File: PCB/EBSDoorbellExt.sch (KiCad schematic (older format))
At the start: 35 parts

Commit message: Completed the initial layout and Gerbers
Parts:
- removed U?: LM555N, symbol LM555N
- added U2: LM555N, Housings_SOIC:SOIC-8_3.9x4.9mm_Pitch1.27mm, symbol LM555N
- C1: renamed from C?; footprint (none) -> Capacitors_ThroughHole:C_Radial_D10_L13_P5
- C10: renamed from C?; footprint 1206 -> Capacitors_SMD:C_1206_HandSoldering
- C2, C3, C5, C6, C7, C8: renamed from C?; footprint (none) -> Capacitors_SMD:C_0805_HandSoldering
- C4, C9: renamed from C?; footprint (none) -> Capacitors_ThroughHole:C_Radial_D5_L11_P2
- D1, D4, D6: renamed from D?; footprint (none) -> Diodes_SMD:SOD-523
- D2: renamed from D?; footprint (none) -> EBSDoorbellExt-Footprints:B80C1500G
- D3, D5: renamed from D?; footprint (none) -> LEDs:LED_0805
- MOD1: renamed from MOD?; footprint (none) -> EBSDoorbellExt-Footprints:BoardConnector_Horizontal_1x2_P5; symbol FS20S4SUB2/4 -> FS20S4SUB2/4-RESCUE-EBSDoorbellExt
- P1: renamed from P?; value CONN_01X02 -> AC in; footprint (none) -> EBSDoorbellExt-Footprints:BoardConnector_Horizontal_1x2_P5; ConradPN (none) -> Value; DigiKeyPN (none) -> Value; Link (none) -> Value; Voltage (none) -> Value
- P2: renamed from P?; value CONN_01X03 -> Doorbell; footprint (none) -> EBSDoorbellExt-Footprints:BoardConnector_Horizontal_1x3_P5; ConradPN (none) -> Value; DigiKeyPN (none) -> Value; Link (none) -> Value; Voltage (none) -> Value
- Q1: renamed from Q?; footprint (none) -> TO_SOT_Packages_SMD:SOT-23
- R1, R10, R2, R3, R4, R5, R6, R7, R8, R9: renamed from R?; footprint (none) -> Resistors_SMD:R_0805_HandSoldering
- REL1: renamed from REL?; footprint (none) -> EBSDoorbellExt-Footprints:MES1A12
- SW1: renamed from SW?; footprint (none) -> Pin_Headers:Pin_Header_Straight_1x02
- SW2: renamed from SW?; footprint (none) -> EBSDoorbellExt-Footprints:FSM2JSMAA
- U1: renamed from U?; footprint TO-220 -> TO_SOT_Packages_THT:TO-220_Neutral123_Vertical
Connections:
- net labels added: In1
- wire segments 85 -> 87
- no-connect marks 3 -> 0
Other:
- moved on the sheet: R6

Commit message: Updated the layout to include the heatsink
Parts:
- removed P2: Doorbell, EBSDoorbellExt-Footprints:BoardConnector_Horizontal_1x3_P5, symbol CONN_01X03
- added P2: Doorbell, EBSDoorbellExt-Footprints:BoardConnector_Horizontal_1x3_P5, symbol Doorbell
- R6: footprint Resistors_SMD:R_0805_HandSoldering -> Resistors_SMD:R_1812_HandSoldering; DigiKeyPN Value -> MF-MSMF050-2CT-ND
- REL1: ConradPN (none) -> Value; DigiKeyPN (none) -> Value; Link (none) -> Value; Voltage (none) -> Value
- U1: value LM7809ACT -> LM7812CT; DigiKeyPN MC7809CTGOS-ND -> LM7812CTFS-ND
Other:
- note added: "Optional"
- moved on the sheet: C7, C8, C9, D4, D6, Q1, R10, R4, R6, R7, R8, R9

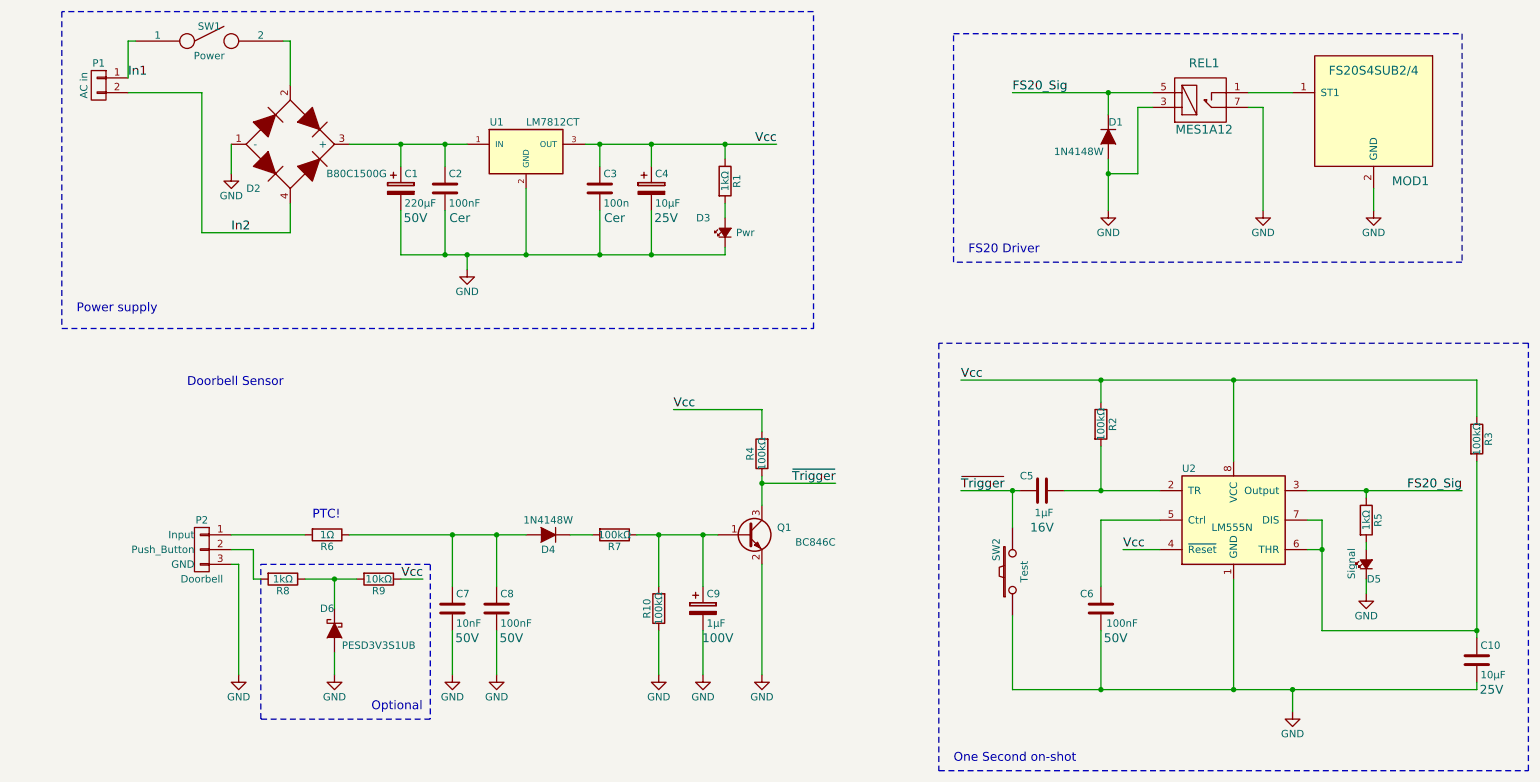
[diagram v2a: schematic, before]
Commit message: Added some test points and moved the LEDs help with the casing
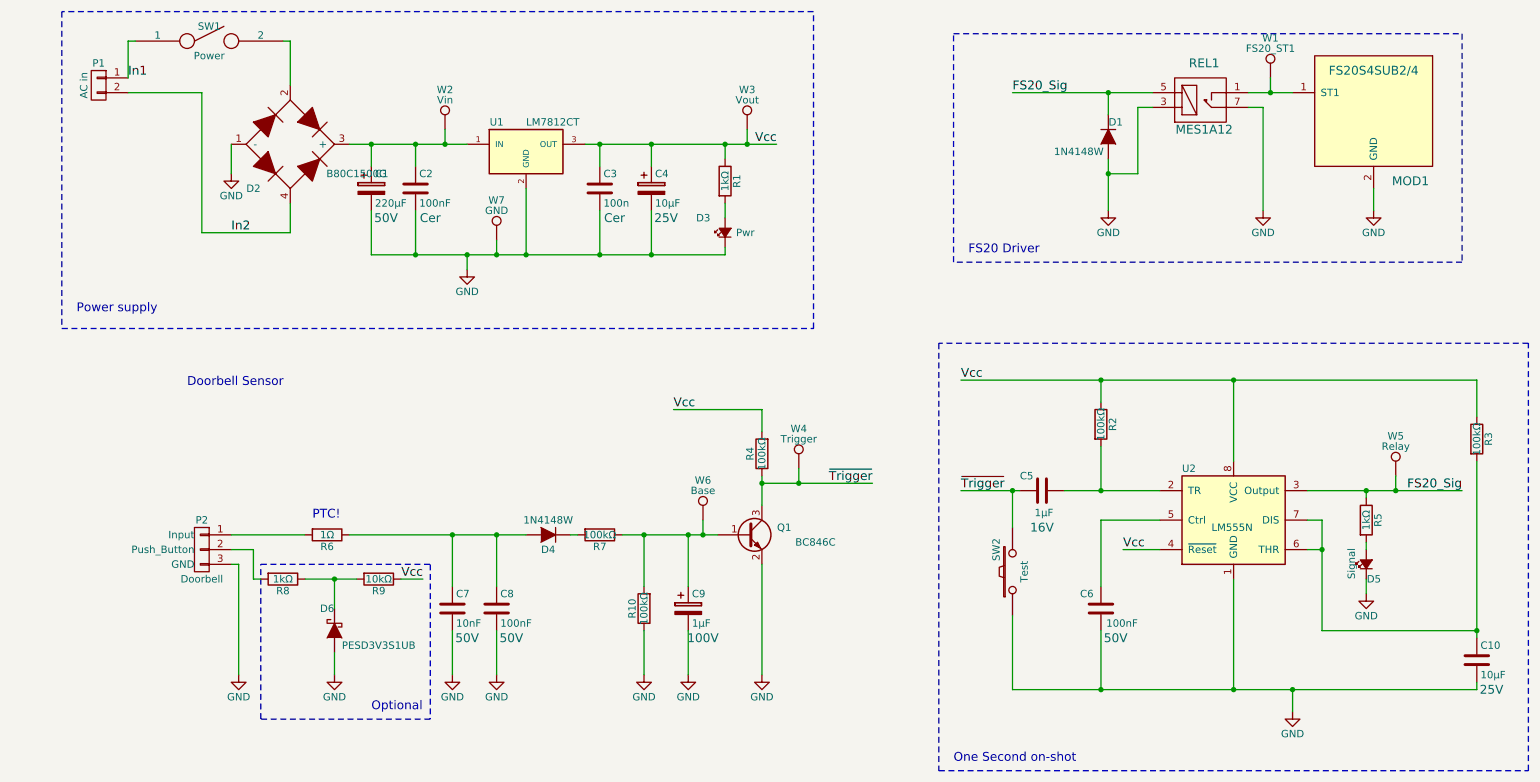
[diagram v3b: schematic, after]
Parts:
- added W1: FS20_ST1, Pin_Headers:Pin_Header_Straight_1x01, symbol TEST_1P
- added W2: Vin, Pin_Headers:Pin_Header_Straight_1x01, symbol TEST_1P
- added W3: Vout, Pin_Headers:Pin_Header_Straight_1x01, symbol TEST_1P
- added W4: Trigger, Pin_Headers:Pin_Header_Straight_1x01, symbol TEST_1P
- added W5: Relay, Pin_Headers:Pin_Header_Straight_1x01, symbol TEST_1P
- added W6: Base, Pin_Headers:Pin_Header_Straight_1x01, symbol TEST_1P
- added W7: GND, Pin_Headers:Pin_Header_Straight_1x01, symbol TEST_1P
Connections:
- net FS20_Sig: now also W5.1
- net GND: now also W7.1
- net Vcc: now also W3.1
- net ~Trigger: now also W4.1
- net at C1.1, C2.1, D2.3 (+)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: now also W2.1
- net at MOD1.1 (ST1), REL1.1: now also W1.1
- net at C9.1, Q1.1 (B), R10.2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: now also W6.1
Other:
- moved on the sheet: C1, C2, C9, R10, R7
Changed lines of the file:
@@
 L CP C1
 U 1 1 57540A4C
-P 2900 1900
-F 0 "C1" H 2925 2000 50  0000 L CNN
-F 1 "220μF" H 2925 1800 50  0000 L CNN
-F 2 "Capacitors_ThroughHole:C_Radial_D10_L13_P5" H 2938 1750 50  0001 C CNN
-F 3 "http://industrial.panasonic.com/www-cgi/jvcr13pz.cgi?E+PZ+3+ABA0012+ECA1HM221+7+WW" H 2900 1900 50  0001 C CNN
-F 4 "P5183-ND" H 2900 1900 60  0001 C CNN "DigiKeyPN"
-F 5 "50V" H 3000 1700 60  0000 C CNN "Voltage"
-F 6 "Value" H 2900 1900 60  0001 C CNN "ConradPN"
-F 7 "Value" H 2900 1900 60  0001 C CNN "Link"
-	1    2900 1900
+P 2700 1900
+F 0 "C1" H 2725 2000 50  0000 L CNN
+F 1 "220μF" H 2725 1800 50  0000 L CNN
+F 2 "Capacitors_ThroughHole:C_Radial_D10_L13_P5" H 2738 1750 50  0001 C CNN
+F 3 "http://industrial.panasonic.com/www-cgi/jvcr13pz.cgi?E+PZ+3+ABA0012+ECA1HM221+7+WW" H 2700 1900 50  0001 C CNN
+F 4 "P5183-ND" H 2700 1900 60  0001 C CNN "DigiKeyPN"
+F 5 "50V" H 2800 1700 60  0000 C CNN "Voltage"
+F 6 "Value" H 2700 1900 60  0001 C CNN "ConradPN"
+F 7 "Value" H 2700 1900 60  0001 C CNN "Link"
+	1    2700 1900
 	1    0    0    -1
 $EndComp
@@
 L C C2
 U 1 1 57540B53
-P 3200 1900
-F 0 "C2" H 3225 2000 50  0000 L CNN
-F 1 "100nF" H 3225 1800 50  0000 L CNN
-F 2 "Capacitors_SMD:C_0805_HandSoldering" H 3238 1750 50  0001 C CNN
-F 3 "" H 3200 1900 50  0000 C CNN
-F 4 "Value" H 3200 1900 60  0001 C CNN "DigiKeyPN"
-F 5 "Cer" H 3300 1700 60  0000 C CNN "Voltage"
-F 6 "Value" H 3200 1900 60  0001 C CNN "ConradPN"
-F 7 "Value" H 3200 1900 60  0001 C CNN "Link"
-	1    3200 1900
+P 3000 1900
+F 0 "C2" H 3025 2000 50  0000 L CNN
+F 1 "100nF" H 3025 1800 50  0000 L CNN
+F 2 "Capacitors_SMD:C_0805_HandSoldering" H 3038 1750 50  0001 C CNN
+F 3 "" H 3000 1900 50  0000 C CNN
+F 4 "Value" H 3000 1900 60  0001 C CNN "DigiKeyPN"
+F 5 "Cer" H 3100 1700 60  0000 C CNN "Voltage"
+F 6 "Value" H 3000 1900 60  0001 C CNN "ConradPN"
+F 7 "Value" H 3000 1900 60  0001 C CNN "Link"
+	1    3000 1900
 	1    0    0    -1
 $EndComp
@@
 Connection ~ 4250 1600
 Wire Wire Line
-	3200 1750 3200 1600
-Connection ~ 3200 1600
-Wire Wire Line
-	2900 1750 2900 1600
-Connection ~ 2900 1600
-Wire Wire Line
-	2900 2050 2900 2350
-Wire Wire Line
-	2900 2350 5100 2350
+	3000 1750 3000 1600
+Connection ~ 3000 1600
+Wire Wire Line
+	2700 1750 2700 1600
+Connection ~ 2700 1600
+Wire Wire Line
+	2700 2050 2700 2350
+Wire Wire Line
+	2700 2350 5100 2350
 Wire Wire Line
 	4600 2350 4600 2050
@@
 Connection ~ 4250 2350
 Wire Wire Line
-	3200 2050 3200 2350
-Connection ~ 3200 2350
+	3000 2050 3000 2350
+Connection ~ 3000 2350
 Wire Wire Line
 	3350 2450 3350 2350
@@
 L R R7
 U 1 1 575476A8
-P 4350 4250
-F 0 "R7" V 4430 4250 50  0000 C CNN
-F 1 "100kΩ" V 4350 4250 50  0000 C CNN
-F 2 "Resistors_SMD:R_0805_HandSoldering" V 4280 4250 50  0001 C CNN
-F 3 "" H 4350 4250 50  0000 C CNN
-	1    4350 4250
+P 4250 4250
+F 0 "R7" V 4330 4250 50  0000 C CNN
+F 1 "100kΩ" V 4250 4250 50  0000 C CNN
+F 2 "Resistors_SMD:R_0805_HandSoldering" V 4180 4250 50  0001 C CNN
+F 3 "" H 4250 4250 50  0000 C CNN
+	1    4250 4250
 	0    1    1    0
 $EndComp
@@
 L R R10
 U 1 1 575477B0
-P 4650 4750
-F 0 "R10" V 4730 4750 50  0000 C CNN
-F 1 "100kΩ" V 4650 4750 50  0000 C CNN
-F 2 "Resistors_SMD:R_0805_HandSoldering" V 4580 4750 50  0001 C CNN
-F 3 "" H 4650 4750 50  0000 C CNN
-	1    4650 4750
+P 4550 4750
+F 0 "R10" V 4630 4750 50  0000 C CNN
+F 1 "100kΩ" V 4550 4750 50  0000 C CNN
+F 2 "Resistors_SMD:R_0805_HandSoldering" V 4480 4750 50  0001 C CNN
+F 3 "" H 4550 4750 50  0000 C CNN
+	1    4550 4750
 	-1   0    0    1
 $EndComp
@@
 L CP C9
 U 1 1 57547833
-P 4950 4750
-F 0 "C9" H 4975 4850 50  0000 L CNN
-F 1 "1μF" H 4975 4650 50  0000 L CNN
-F 2 "Capacitors_ThroughHole:C_Radial_D5_L11_P2" H 4988 4600 50  0001 C CNN
-F 3 "http://nichicon-us.com/english/products/pdfs/e-ups.pdf" H 4950 4750 50  0001 C CNN
-F 4 "493-5378-1-ND" H 4950 4750 60  0001 C CNN "DigiKeyPN"
-F 5 "100V" H 5050 4550 60  0000 C CNN "Voltage"
-F 6 "Value" H 4950 4750 60  0001 C CNN "ConradPN"
-F 7 "Value" H 4950 4750 60  0001 C CNN "Link"
-	1    4950 4750
+P 4850 4750
+F 0 "C9" H 4875 4850 50  0000 L CNN
+F 1 "1μF" H 4875 4650 50  0000 L CNN
+F 2 "Capacitors_ThroughHole:C_Radial_D5_L11_P2" H 4888 4600 50  0001 C CNN
+F 3 "http://nichicon-us.com/english/products/pdfs/e-ups.pdf" H 4850 4750 50  0001 C CNN
+F 4 "493-5378-1-ND" H 4850 4750 60  0001 C CNN "DigiKeyPN"
+F 5 "100V" H 4950 4550 60  0000 C CNN "Voltage"
+F 6 "Value" H 4850 4750 60  0001 C CNN "ConradPN"
+F 7 "Value" H 4850 4750 60  0001 C CNN "Link"
+	1    4850 4750
 	1    0    0    -1
 $EndComp
@@
 	2550 4250 3750 4250
 Wire Wire Line
-	4050 4250 4200 4250
-Wire Wire Line
-	4500 4250 5050 4250
+	4050 4250 4100 4250
+Wire Wire Line
+	4400 4250 5050 4250
 Wire Wire Line
 	5350 3850 5350 4050
@@
 	3550 5200 3550 4900
 Wire Wire Line
-	4650 4600 4650 4250
-Connection ~ 4650 4250
-Wire Wire Line
-	4950 4600 4950 4250
-Connection ~ 4950 4250
+	4550 4600 4550 4250
+Connection ~ 4550 4250
+Wire Wire Line
+	4850 4600 4850 4250
+Connection ~ 4850 4250
 $Comp
 L GND #PWR011
 U 1 1 5754947D
-P 4650 5200
-F 0 "#PWR011" H 4650 4950 50  0001 C CNN
-F 1 "GND" H 4650 5050 50  0000 C CNN
-F 2 "" H 4650 5200 50  0000 C CNN
-F 3 "" H 4650 5200 50  0000 C CNN
-	1    4650 5200
+P 4550 5200
+F 0 "#PWR011" H 4550 4950 50  0001 C CNN
+F 1 "GND" H 4550 5050 50  0000 C CNN
+F 2 "" H 4550 5200 50  0000 C CNN
+F 3 "" H 4550 5200 50  0000 C CNN
+	1    4550 5200
 	1    0    0    -1
 $EndComp
@@
 L GND #PWR012
 U 1 1 57549484
-P 4950 5200
-F 0 "#PWR012" H 4950 4950 50  0001 C CNN
-F 1 "GND" H 4950 5050 50  0000 C CNN
-F 2 "" H 4950 5200 50  0000 C CNN
-F 3 "" H 4950 5200 50  0000 C CNN
-	1    4950 5200
-	1    0    0    -1
-$EndComp
-Wire Wire Line
-	4950 5200 4950 4900
-Wire Wire Line
-	4650 4900 4650 5200
+P 4850 5200
+F 0 "#PWR012" H 4850 4950 50  0001 C CNN
+F 1 "GND" H 4850 5050 50  0000 C CNN
+F 2 "" H 4850 5200 50  0000 C CNN
+F 3 "" H 4850 5200 50  0000 C CNN
+	1    4850 5200
+	1    0    0    -1
+$EndComp
+Wire Wire Line
+	4850 5200 4850 4900
+Wire Wire Line
+	4550 4900 4550 5200
 $Comp
 L GND #PWR013
@@
 Wire Wire Line
 	1800 4450 1800 5200
-Text Label 5850 3900 2    60   ~ 0
+Text Label 6100 3900 2    60   ~ 0
 ~Trigger
 $Comp
@@
 	5350 3550 5350 3400
 Wire Wire Line
-	5350 3900 5850 3900
+	5350 3900 6100 3900
 Connection ~ 5350 3900
 Wire Wire Line
@@
 	-1   0    0    -1
 $EndComp
+$Comp
+L TEST_1P W3
+U 1 1 5757086F
+P 5250 1500
+F 0 "W3" H 5250 1770 50  0000 C CNN
+F 1 "Vout" H 5250 1700 50  0000 C CNN
+F 2 "Pin_Headers:Pin_Header_Straight_1x01" H 5450 1500 50  0001 C CNN
+F 3 "" H 5450 1500 50  0000 C CNN
+	1    5250 1500
+	1    0    0    -1
+$EndComp
+$Comp
+L TEST_1P W1
+U 1 1 57570A06
+P 8800 1150
+F 0 "W1" H 8800 1420 50  0000 C CNN
+F 1 "FS20_ST1" H 8800 1350 50  0000 C CNN
+F 2 "Pin_Headers:Pin_Header_Straight_1x01" H 9000 1150 50  0001 C CNN
+F 3 "" H 9000 1150 50  0000 C CNN
+	1    8800 1150
+	1    0    0    -1
+$EndComp
+$Comp
+L TEST_1P W5
+U 1 1 57570B03
+P 9650 3850
+F 0 "W5" H 9650 4120 50  0000 C CNN
+F 1 "Relay" H 9650 4050 50  0000 C CNN
+F 2 "Pin_Headers:Pin_Header_Straight_1x01" H 9850 3850 50  0001 C CNN
+F 3 "" H 9850 3850 50  0000 C CNN
+	1    9650 3850
+	1    0    0    -1
+$EndComp
+$Comp
+L TEST_1P W2
+U 1 1 57570C5A
+P 3200 1500
+F 0 "W2" H 3200 1770 50  0000 C CNN
+F 1 "Vin" H 3200 1700 50  0000 C CNN
+F 2 "Pin_Headers:Pin_Header_Straight_1x01" H 3400 1500 50  0001 C CNN
+F 3 "" H 3400 1500 50  0000 C CNN
+	1    3200 1500
+	1    0    0    -1
+$EndComp
+$Comp
+L TEST_1P W4
+U 1 1 57570D3E
+P 5600 3800
+F 0 "W4" H 5600 4070 50  0000 C CNN
+F 1 "Trigger" H 5600 4000 50  0000 C CNN
+F 2 "Pin_Headers:Pin_Header_Straight_1x01" H 5800 3800 50  0001 C CNN
+F 3 "" H 5800 3800 50  0000 C CNN
+	1    5600 3800
+	1    0    0    -1
+$EndComp
+$Comp
+L TEST_1P W6
+U 1 1 57570E0E
+P 4950 4150
+F 0 "W6" H 4950 4420 50  0000 C CNN
+F 1 "Base" H 4950 4350 50  0000 C CNN
+F 2 "Pin_Headers:Pin_Header_Straight_1x01" H 5150 4150 50  0001 C CNN
+F 3 "" H 5150 4150 50  0000 C CNN
+	1    4950 4150
+	1    0    0    -1
+$EndComp
+Wire Wire Line
+	8800 1150 8800 1250
+Connection ~ 8800 1250
+Wire Wire Line
+	9650 3850 9650 3950
+Connection ~ 9650 3950
+Wire Wire Line
+	5600 3800 5600 3900
+Connection ~ 5600 3900
+Wire Wire Line
+	5250 1500 5250 1600
+Connection ~ 5250 1600
+Wire Wire Line
+	3200 1500 3200 1600
+Connection ~ 3200 1600
+Wire Wire Line
+	4950 4150 4950 4250
+Connection ~ 4950 4250
+$Comp
+L TEST_1P W7
+U 1 1 57573295
+P 3550 2250
+F 0 "W7" H 3550 2520 50  0000 C CNN
+F 1 "GND" H 3550 2450 50  0000 C CNN
+F 2 "Pin_Headers:Pin_Header_Straight_1x01" H 3750 2250 50  0001 C CNN
+F 3 "" H 3750 2250 50  0000 C CNN
+	1    3550 2250
+	1    0    0    -1
+$EndComp
+Wire Wire Line
+	3550 2250 3550 2350
+Connection ~ 3550 2350
 $EndSCHEMATC
